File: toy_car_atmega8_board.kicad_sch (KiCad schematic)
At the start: 9 parts, among them J1 Conn_01x06_Pin, J2 Conn_01x08_Pin, J3 Conn_01x06_Pin, J4 Conn_01x06_Pin, J5 Conn_01x02_Pin, U1 ATmega8A-P, Y1 Crystal

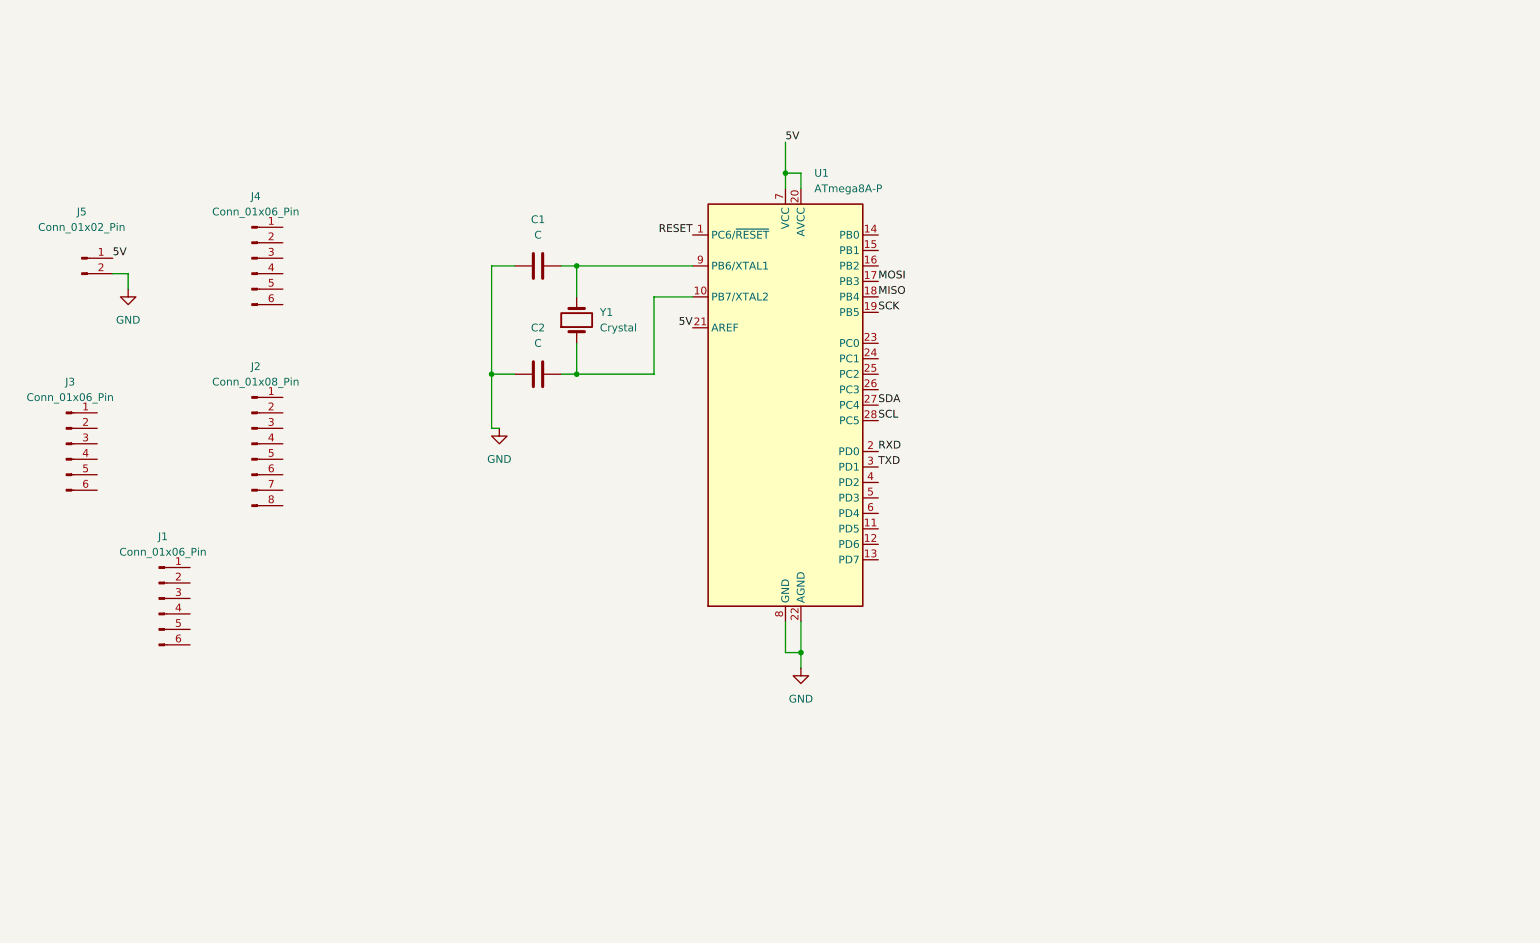
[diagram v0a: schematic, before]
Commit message: Added all labels, capacitors, resiatnce and push buttton.
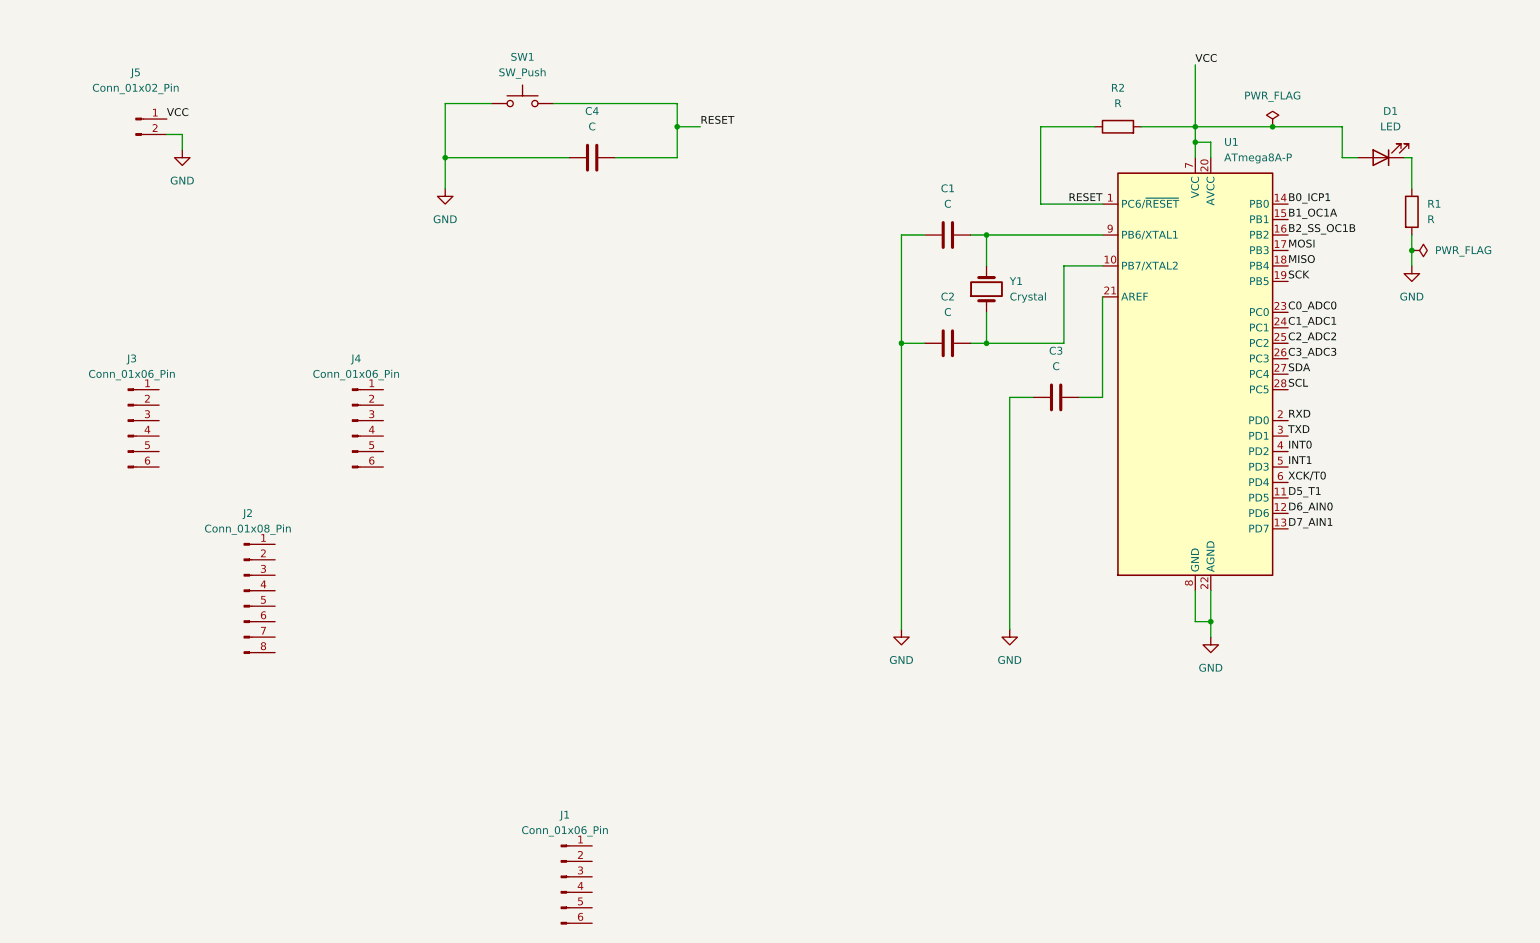
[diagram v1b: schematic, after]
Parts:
- added C3, C4: C, symbol Device:C
- added D1: LED, symbol Device:LED
- added R1, R2: R, symbol Device:R
- added SW1: SW_Push, symbol Switch:SW_Push
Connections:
- net GND: now also C3.1, C4.1, R1.2, SW1.1
- net RESET: now also C4.2, R2.1, SW1.2
- net D5_T1: now reaches U1.11 (PD5)
- net D6_AIN0: now reaches U1.12 (PD6)
- net D7_AIN1: now reaches U1.13 (PD7)
- net B0_ICP1: now reaches U1.14 (PB0)
- net B1_OC1A: now reaches U1.15 (PB1)
- net B2_SS_OC1B: now reaches U1.16 (PB2)
- net C0_ADC0: now reaches U1.23 (PC0)
- net C1_ADC1: now reaches U1.24 (PC1)
- net C2_ADC2: now reaches U1.25 (PC2)
- net C3_ADC3: now reaches U1.26 (PC3)
- net INT0: now reaches U1.4 (PD2)
- net INT1: now reaches U1.5 (PD3)
- net XCK/T0: now reaches U1.6 (PD4)
- net 5V renamed VCC
- net VCC: now also D1.2 (A), R2.2; no longer U1.21 (AREF)
- new net: D1.1 (K), R1.1
- new net: C3.2, U1.21 (AREF)
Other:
- moved on the sheet: C1, C2, J1, J2, J3, J4, J5, U1, Y1

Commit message: Added footprints and value, checked electrical connections. All good
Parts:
- added C5: 0.1uF, Capacitor_THT:C_Disc_D3.8mm_W2.6mm_P2.50mm, symbol Device:C
- C1, C2: value C -> 22pF; footprint (none) -> Capacitor_THT:C_Disc_D3.8mm_W2.6mm_P2.50mm
- C3: value C -> 0.1uF; footprint (none) -> Capacitor_THT:C_Disc_D3.8mm_W2.6mm_P2.50mm
- C4: value C -> 100nF; footprint (none) -> Capacitor_THT:C_Disc_D3.8mm_W2.6mm_P2.50mm
- D1: footprint (none) -> LED_THT:LED_D3.0mm
- J1, J3, J4: footprint (none) -> Connector_PinHeader_2.54mm:PinHeader_1x06_P2.54mm_Vertical
- J2: footprint (none) -> Connector_PinHeader_2.54mm:PinHeader_1x08_P2.54mm_Vertical
- J5: footprint (none) -> Connector_PinHeader_2.54mm:PinHeader_1x02_P2.54mm_Vertical
- R1: value R -> 330; footprint (none) -> Resistor_THT:R_Axial_DIN0207_L6.3mm_D2.5mm_P7.62mm_Horizontal
- R2: value R -> 10k; footprint (none) -> Resistor_THT:R_Axial_DIN0207_L6.3mm_D2.5mm_P7.62mm_Horizontal
- SW1: footprint (none) -> Button_Switch_THT:SW_PUSH_6mm
- Y1: value Crystal -> 16Mhz; footprint (none) -> Crystal:Crystal_HC18-U_Vertical
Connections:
- net B0_ICP1: now also J3.1 (Pin_1)
- net B1_OC1A: now also J3.2 (Pin_2)
- net B2_SS_OC1B: now also J3.3 (Pin_3)
- net C0_ADC0: now also J4.1 (Pin_1)
- net C1_ADC1: now also J4.2 (Pin_2)
- net C2_ADC2: now also J4.3 (Pin_3)
- net C3_ADC3: now also J4.4 (Pin_4)
- net D5_T1: now also J2.6 (Pin_6)
- net D6_AIN0: now also J2.7 (Pin_7)
- net D7_AIN1: now also J2.8 (Pin_8)
- net GND: now also J1.6 (Pin_6), C5.1
- net INT0: now also J2.3 (Pin_3)
- net INT1: now also J2.4 (Pin_4)
- net MISO: now also J1.4 (Pin_4), J3.5 (Pin_5)
- net MOSI: now also J1.3 (Pin_3), J3.4 (Pin_4)
- net RESET: now also J1.2 (Pin_2)
- net RXD: now also J2.1 (Pin_1)
- net SCK: now also J1.5 (Pin_5), J3.6 (Pin_6)
- net SCL: now also J4.6 (Pin_6)
- net SDA: now also J4.5 (Pin_5)
- net TXD: now also J2.2 (Pin_2)
- net VCC: now also C3.2, J1.1 (Pin_1), U1.21 (AREF), C5.2
- net XCK/T0: now also J2.5 (Pin_5)
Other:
- note added: "Atmega8 uC"
- note added: "GPIO pins"
- note added: "ISP programmer pins"
- note added: "Power Supply"
- note added: "Reset Push btn"
- company: (none) -> R.K hobbyst
- title: (none) -> Toy car microcontroller
- moved on the sheet: C1, C2, C3, C4, D1, J1, J2, J3, J4, J5, R1, R2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

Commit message: Completed pcb design and routing.
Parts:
- C4: value 100nF -> 0.1uF
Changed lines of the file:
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@@
       (effects (font (size 1.27 1.27)))
     )
-    (property "Value" "100nF" (at 91.44 40.64 90)
+    (property "Value" "0.1uF" (at 91.44 40.64 90)
       (effects (font (size 1.27 1.27)))
     )

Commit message: Updated pcb
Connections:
- net RESET: now also J1.1 (Pin_1); no longer J1.2 (Pin_2)
- net VCC: now also J1.2 (Pin_2); no longer J1.1 (Pin_1)
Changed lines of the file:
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@@
     (effects (font (size 1.27 1.27)) (justify left bottom))
   )
-  (label "RESET" (at 113.03 146.05 0) (fields_autoplaced)
+  (label "RESET" (at 113.03 143.51 0) (fields_autoplaced)
     (effects (font (size 1.27 1.27)) (justify left bottom))
   )
@@
     (effects (font (size 1.27 1.27)) (justify left bottom))
   )
-  (label "VCC" (at 113.03 143.51 0) (fields_autoplaced)
+  (label "VCC" (at 113.03 146.05 0) (fields_autoplaced)
     (effects (font (size 1.27 1.27)) (justify left bottom))
   )
